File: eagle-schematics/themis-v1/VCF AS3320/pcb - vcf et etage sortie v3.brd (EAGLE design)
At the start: 78 x 63.8 mm, 42 parts

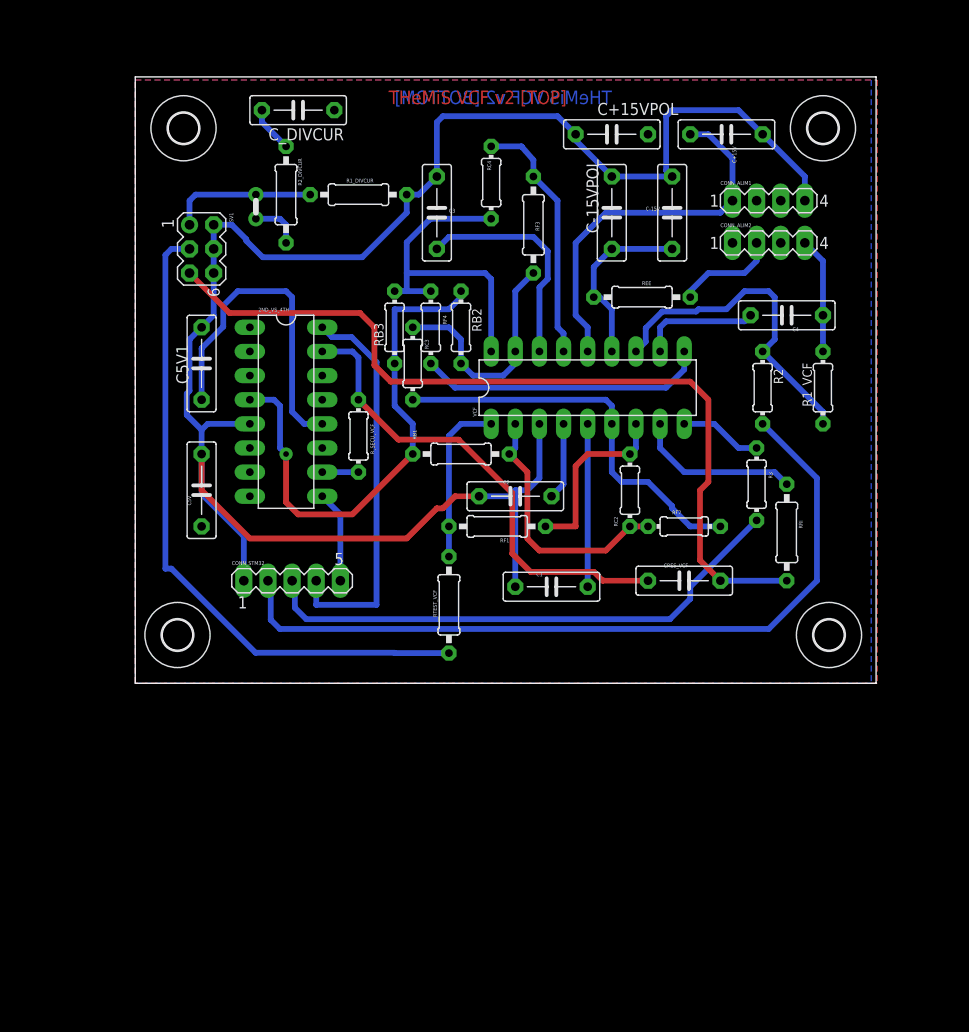
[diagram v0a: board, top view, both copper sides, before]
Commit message: Improved schematics, added analog chips library
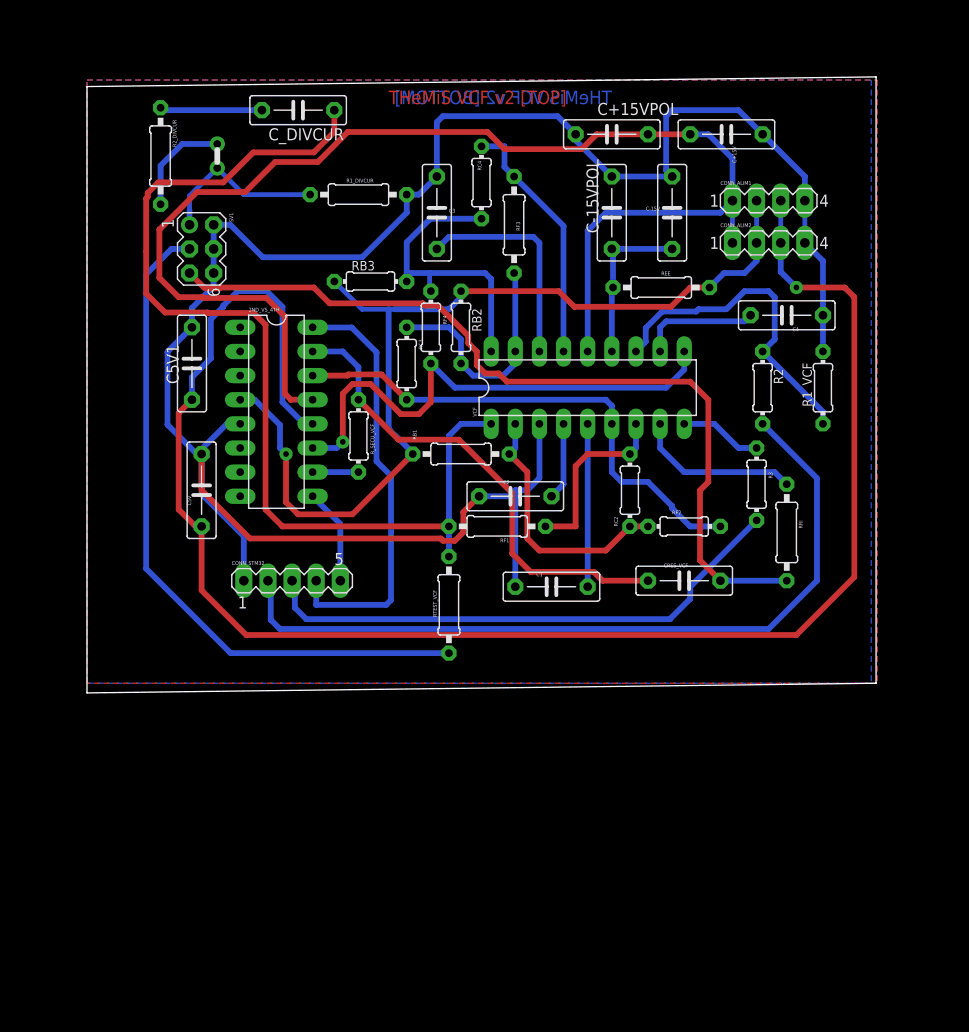
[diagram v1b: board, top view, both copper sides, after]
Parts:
- removed U$1, U$2, U$3, U$4: (no value), holes:3,2
- moved R2_DIVCUR 13.8 mm to (0.13, 50.4)
- moved JP_MIXER_OUT 6.71 mm to (6.10, 50.4), turned to 90 degrees
- moved RB3 5.45 mm to (22.2, 37.2), turned to 0 degrees
- moved REE 2.27 mm to (52.8, 36.6)
- moved RF3 2.03 mm to (37.3, 43.2)
- moved C5V1 1.02 mm to (3.43, 28.6)
- moved 2ND_VS_4TH 1.02 mm to (12.3, 23.5)
- moved RC4 1.02 mm to (33.9, 47.6)
- moved RC3 0.64 mm to (26.0, 28.6)
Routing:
- net 5V: track 34.8 -> 174.0 mm, vias 0 -> 1
- net +15V: track 40.2 -> 136.5 mm
- net VCF_IN: track 17.7 -> 106.3 mm
- net -15V: track 65.4 -> 102.3 mm
- net N$69: track 30.4 -> 54.5 mm, vias 0 -> 1
- net N$65: track 42.1 -> 53.8 mm
- net AGND: track 208.7 -> 217.0 mm
- net N$75: track 4.86 -> 10.8 mm
- net N$79: track 5.34 -> 11.0 mm
- net N$83: track 35.7 -> 32.0 mm
- net IN_2NDORDER: track 42.3 -> 45.8 mm
- net V_IN: track 69.4 -> 72.2 mm
- net I_IN: track 15.5 -> 18.1 mm
- net VM3320: track 19.1 -> 17.3 mm
- net N$73: track 3.81 -> 4.83 mm
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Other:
- board size 78 x 63.8 mm -> 83.1 x 64.8 mm

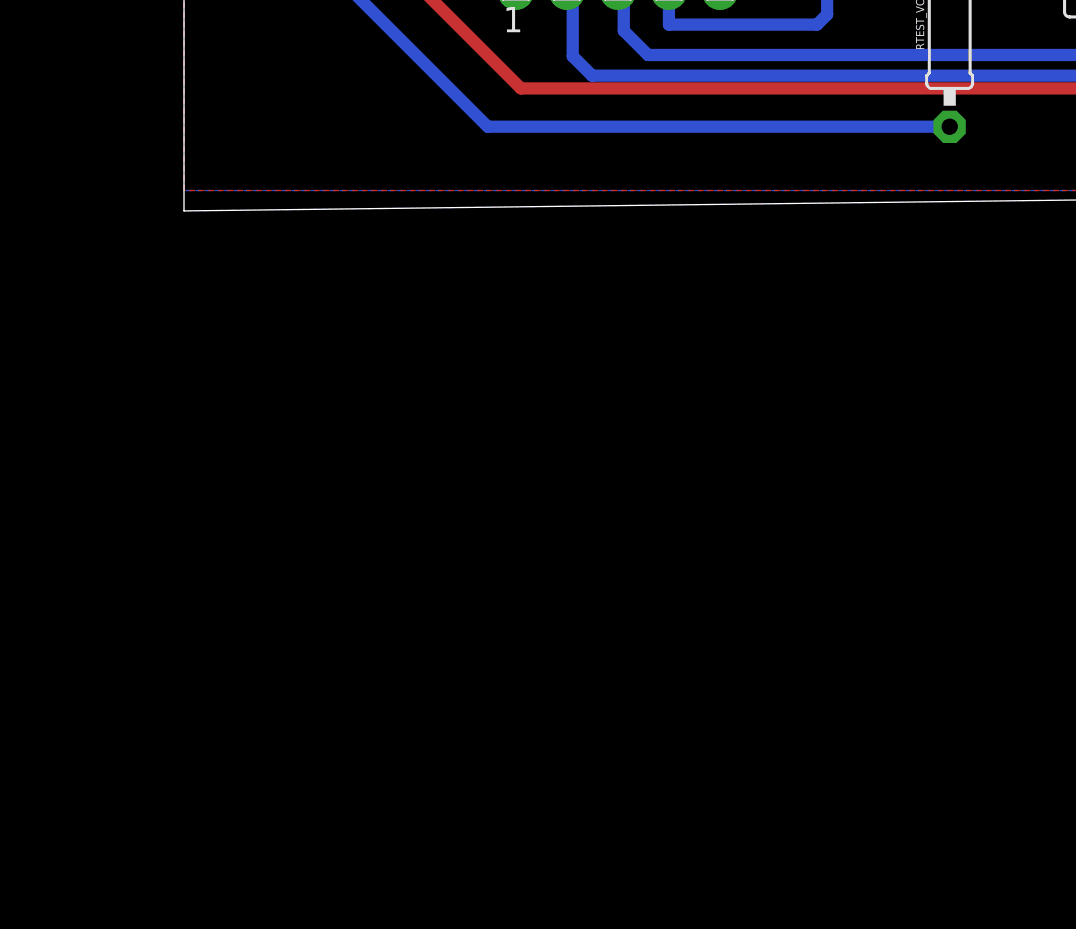
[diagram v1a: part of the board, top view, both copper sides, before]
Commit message: New version of DAC board based on AD5391 chip
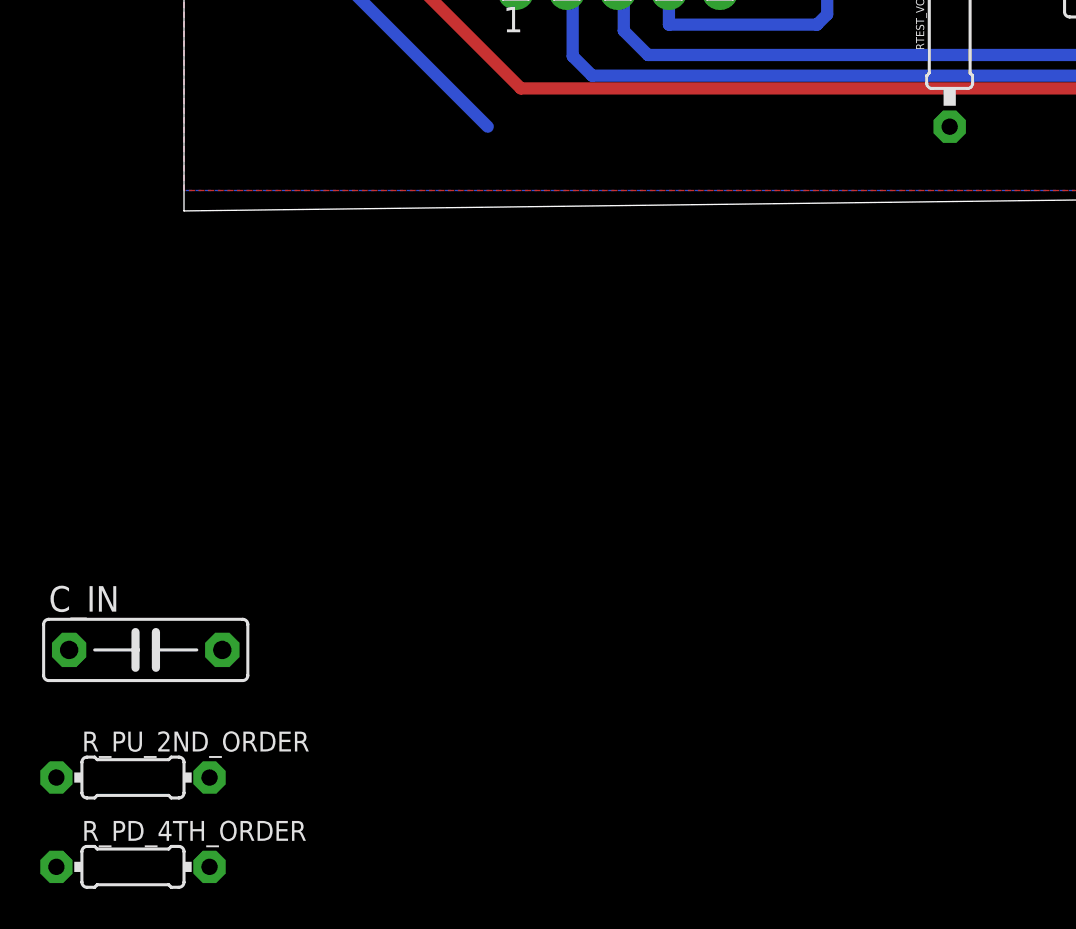
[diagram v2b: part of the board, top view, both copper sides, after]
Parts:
- added C_IN: 470n, rcl:C075-032X103
- added R_PD_4TH_ORDER, R_PU_2ND_ORDER: 100k, rcl:0204/7
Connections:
- new net GND: R_PD_4TH_ORDER.1
- new net N$1: C_IN.1, RTEST_VCF.1
- net 5V: now also R_PU_2ND_ORDER.1
- net IN_2NDORDER: now also R_PU_2ND_ORDER.2
- net IN_4THORDER: now also R_PD_4TH_ORDER.2
- net V_IN: now also C_IN.2; no longer RTEST_VCF.1
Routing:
- net V_IN: track 72.2 -> 49.2 mm
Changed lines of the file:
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@@
 <?xml version="1.0" encoding="utf-8"?>
 <!DOCTYPE eagle SYSTEM "eagle.dtd">
-<eagle version="9.5.0">
+<eagle version="9.5.2">
 <drawing>
 <settings>
@@
 <attribute name="VALUE" x="19.431" y="58.293" size="1.27" layer="27" ratio="10" rot="R180"/>
 </element>
+<element name="C_IN" library="rcl" library_urn="urn:adsk.eagle:library:334" package="C075-032X103" package3d_urn="urn:adsk.eagle:package:23646/1" value="470n" x="-9.525" y="-27.94" smashed="yes">
+<attribute name="NAME" x="-14.351" y="-26.035" size="1.27" layer="25" ratio="10"/>
+<attribute name="SPICEPREFIX" value="C" x="-9.525" y="-27.94" size="1.778" layer="27" display="off"/>
+<attribute name="VALUE" x="-14.351" y="-30.988" size="1.27" layer="27" ratio="10"/>
+</element>
+<element name="R_PU_2ND_ORDER" library="rcl" library_urn="urn:adsk.eagle:library:334" package="0204/7" package3d_urn="urn:adsk.eagle:package:23498/2" value="100k" x="-10.16" y="-34.29" smashed="yes">
+<attribute name="NAME" x="-12.7" y="-32.9946" size="0.9906" layer="25" ratio="10"/>
+<attribute name="SPICEPREFIX" value="R" x="-10.16" y="-34.29" size="1.778" layer="27" display="off"/>
+<attribute name="VALUE" x="-11.7856" y="-34.7726" size="0.9906" layer="27" ratio="10"/>
+</element>
+<element name="R_PD_4TH_ORDER" library="rcl" library_urn="urn:adsk.eagle:library:334" package="0204/7" package3d_urn="urn:adsk.eagle:package:23498/2" value="100k" x="-10.16" y="-38.735" smashed="yes">
+<attribute name="NAME" x="-12.7" y="-37.4396" size="0.9906" layer="25" ratio="10"/>
+<attribute name="SPICEPREFIX" value="R" x="-10.16" y="-38.735" size="1.778" layer="27" display="off"/>
+<attribute name="VALUE" x="-11.7856" y="-39.2176" size="0.9906" layer="27" ratio="10"/>
+</element>
 </elements>
 <signals>
@@
 <wire x1="6.7246" y1="34.544" x2="5.422503125" y2="33.241903125" width="0.6096" layer="16"/>
 <wire x1="5.422503125" y1="33.241903125" x2="5.422503125" y2="29.121496875" width="0.6096" layer="16"/>
+<contactref element="R_PU_2ND_ORDER" pad="1"/>
+<wire x1="4.445" y1="11.43" x2="-13.97" y2="-34.29" width="0" layer="19" extent="1-1"/>
 </signal>
 <signal name="VCF_IN">
@@
 <wire x1="24.384" y1="16.764" x2="24.384" y2="3.683" width="0.6096" layer="16"/>
 <wire x1="16.51" y1="5.715" x2="16.51" y2="3.175" width="0.6096" layer="16"/>
+<contactref element="R_PU_2ND_ORDER" pad="2"/>
+<wire x1="16.51" y1="5.08" x2="-6.35" y2="-34.29" width="0" layer="19" extent="16-16"/>
 </signal>
 <signal name="IN_4THORDER">
@@
 <wire x1="16.129" y1="14.605" x2="19.05" y2="11.684" width="0.6096" layer="16"/>
 <wire x1="19.05" y1="11.684" x2="19.05" y2="5.715" width="0.6096" layer="16"/>
+<contactref element="R_PD_4TH_ORDER" pad="2"/>
+<wire x1="19.05" y1="5.715" x2="-6.35" y2="-38.735" width="0" layer="19" extent="1-1"/>
 </signal>
 <signal name="CV_RES">
@@
 </signal>
 <signal name="V_IN">
-<contactref element="RTEST_VCF" pad="1"/>
 <contactref element="SV1" pad="3"/>
 <wire x1="3.175" y1="40.64" x2="1.27" y2="40.64" width="0.6096" layer="16"/>
 <wire x1="1.27" y1="40.64" x2="-1.397" y2="37.973" width="0.6096" layer="16"/>
 <wire x1="-1.397" y1="6.985" x2="-1.397" y2="37.973" width="0.6096" layer="16"/>
-<wire x1="30.48" y1="-1.905" x2="7.493" y2="-1.905" width="0.6096" layer="16"/>
 <wire x1="7.493" y1="-1.905" x2="-1.397" y2="6.985" width="0.6096" layer="16"/>
+<contactref element="C_IN" pad="2"/>
+<wire x1="7.493" y1="-1.905" x2="-5.715" y2="-27.94" width="0" layer="19" extent="16-16"/>
 </signal>
 <signal name="OUT">
@@
 <wire x1="6.47184375" y1="36.576" x2="6.38304375" y2="36.4872" width="0.6096" layer="1"/>
 </signal>
+<signal name="N$1">
+<contactref element="RTEST_VCF" pad="1"/>
+<contactref element="C_IN" pad="1"/>
+<wire x1="30.48" y1="-1.905" x2="-13.335" y2="-27.94" width="0" layer="19" extent="1-1"/>
+</signal>
+<signal name="GND">
+<contactref element="R_PD_4TH_ORDER" pad="1"/>
+</signal>
 </signals>

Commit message: checked connections
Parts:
- moved R_PD_4TH_ORDER 56.3 mm to (26.0, 4.45), turned to 180 degrees
- moved C_IN 55.7 mm to (-2.54, 27.3), turned to 90 degrees
- moved R_PU_2ND_ORDER 47.4 mm to (10.8, 8.26)
- moved RTEST_VCF 2.54 mm to (33.0, 3.17)
- moved CONN_STM32 1.27 mm to (14.0, 4.45)
- renumbered R1_VCF to R1_CV, R2 to R2_CV, R3 to R_RES
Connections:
- net N$17 renamed VCAP3
- net N$18 renamed VCAP2
- net N$24 renamed VCAP4
- net N$37 renamed VCF_FREQ_CV
- net N$5 renamed VCAP1
- net N$57 renamed OUT1
- net N$62 renamed IN2
- net N$65 renamed OUT2
- net N$69 renamed OUT4
- net N$72 renamed IN3
- net N$82 renamed OUT3
- net N$83 renamed IN4
- net N$86 renamed VIN_RES
- net N$87 renamed VCF_RES_CUR
- net VM3320 renamed VEE
- removed net GND: R_PD_4TH_ORDER.1
- net AGND: now also R_PD_4TH_ORDER.1
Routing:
- net N$1: track 0.00 -> 53.5 mm
- net V_IN: track 49.2 -> 13.0 mm
- net AGND: track 217.0 -> 226.2 mm
- net IN_2NDORDER: track 45.8 -> 50.3 mm
- net IN_4THORDER: track 10.1 -> 14.5 mm
- net 5V: track 174.0 -> 176.5 mm
- net VCF_IN: track 106.3 -> 107.4 mm

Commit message: schematic fix
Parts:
- moved C+15V 9.92 mm to (67.3, 59.1)
- moved RC4 9.92 mm to (41.5, 54.0)
- moved RF2 9.92 mm to (62.9, 17.8)
- moved C1 9.92 mm to (48.9, 11.4)
- moved CRES_VCF 9.92 mm to (62.9, 12.1)
- moved C_DIVCUR 9.92 mm to (22.2, 61.6)
- moved R1_CV 9.92 mm to (77.5, 32.4)
- moved R1_DIVCUR 9.92 mm to (28.6, 52.7)
- moved R2_CV 9.92 mm to (71.1, 32.4)
- moved RF4 9.92 mm to (36.2, 38.7)
- moved R_SECU_VCF 9.92 mm to (28.6, 27.3)
- moved C5V 9.92 mm to (12.1, 21.6)
- moved CONN_STM32 9.92 mm to (21.6, 10.8)
- moved C_IN 9.92 mm to (5.08, 33.7)
- moved JP_MIXER_OUT 9.92 mm to (13.7, 56.8)
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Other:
- board size 83.1 x 64.8 mm -> 82.9 x 64.6 mm
